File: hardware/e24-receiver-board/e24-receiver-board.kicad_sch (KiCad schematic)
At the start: 21 parts, among them J1 505070-2422, J10 SPEAKER-, J11 GND1, J12 TRACK_RIGHT, J13 MOTOR+, J14 LAMP_REAR, J15 CAP+, J16 U+, J17 AUX3, J18 AUX10, J19 AUX12, J2 TRACK_LEFT, J20 SPEAKER+, J21 GND2, J3 MOTOR-, J4 LAMP_FRONT, J5 VCC, J6 AUX1, J7 AUX2, J8 AUX4, J9 AUX11

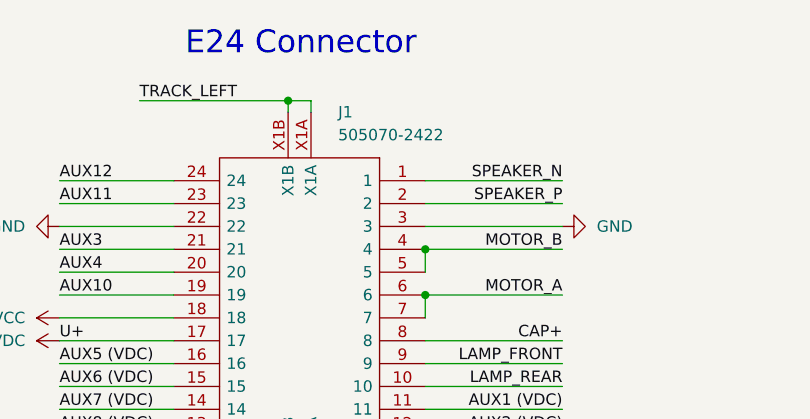
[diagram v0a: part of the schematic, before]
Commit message: fix: update connector part number
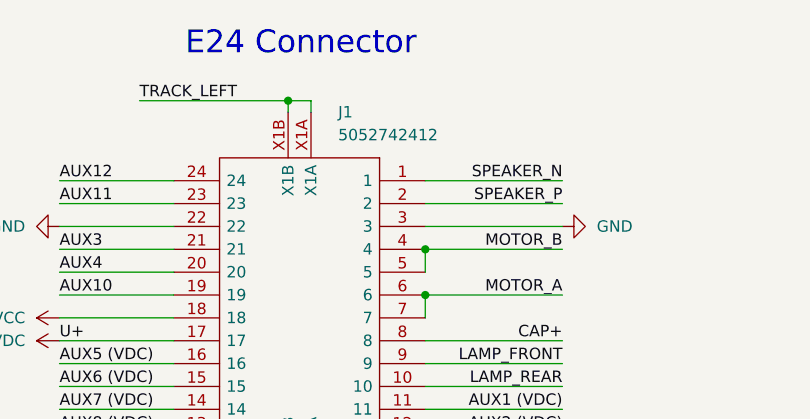
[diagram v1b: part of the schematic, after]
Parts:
- J1: value 505070-2422 -> 5052742412; LCSC C724143 -> C3649712; Manufacturer_Name Molex -> (none); Manufacturer_Part_Number 505070-2422 -> (none)
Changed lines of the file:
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@@
 			)
 		)
-		(property "Value" "505070-2422"
+		(property "Value" "5052742412"
 			(at 80.4865 34.29 90)
 			(effects
@@
 			)
 		)
-		(property "Datasheet" "https://componentsearchengine.com/Datasheets/1/505070-2422.pdf"
+		(property "Datasheet" "https://componentsearchengine.com/Datasheets/1/505274-2412.pdf"
 			(at 82.55 71.12 0)
 			(effects
@@
 			)
 		)
-		(property "Manufacturer_Name" "Molex"
-			(at 69.85 71.12 0)
-			(effects
-				(font
-					(size 1.27 1.27)
-				)
-				(justify left)
-				(hide yes)
-			)
-		)
-		(property "Manufacturer_Part_Number" "505070-2422"
-			(at 67.31 71.12 0)
-			(effects
-				(font
-					(size 1.27 1.27)
-				)
-				(justify left)
-				(hide yes)
-			)
-		)
-		(property "LCSC" "C724143"
+		(property "LCSC" "C3649712"
 			(at 77.47 31.75 90)
 			(effects
